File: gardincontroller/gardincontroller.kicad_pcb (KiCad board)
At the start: 2 copper layers, 26.8 x 41 mm, 24 parts, among them J1 Conn_01x04_Male, J2 USB_C_Receptacle_USB2.0, J3 Conn_01x10_Male, J4 Conn_01x06_Male, U1 ESP32-S2-MINI-1-N4, U2 LM1117-3.3

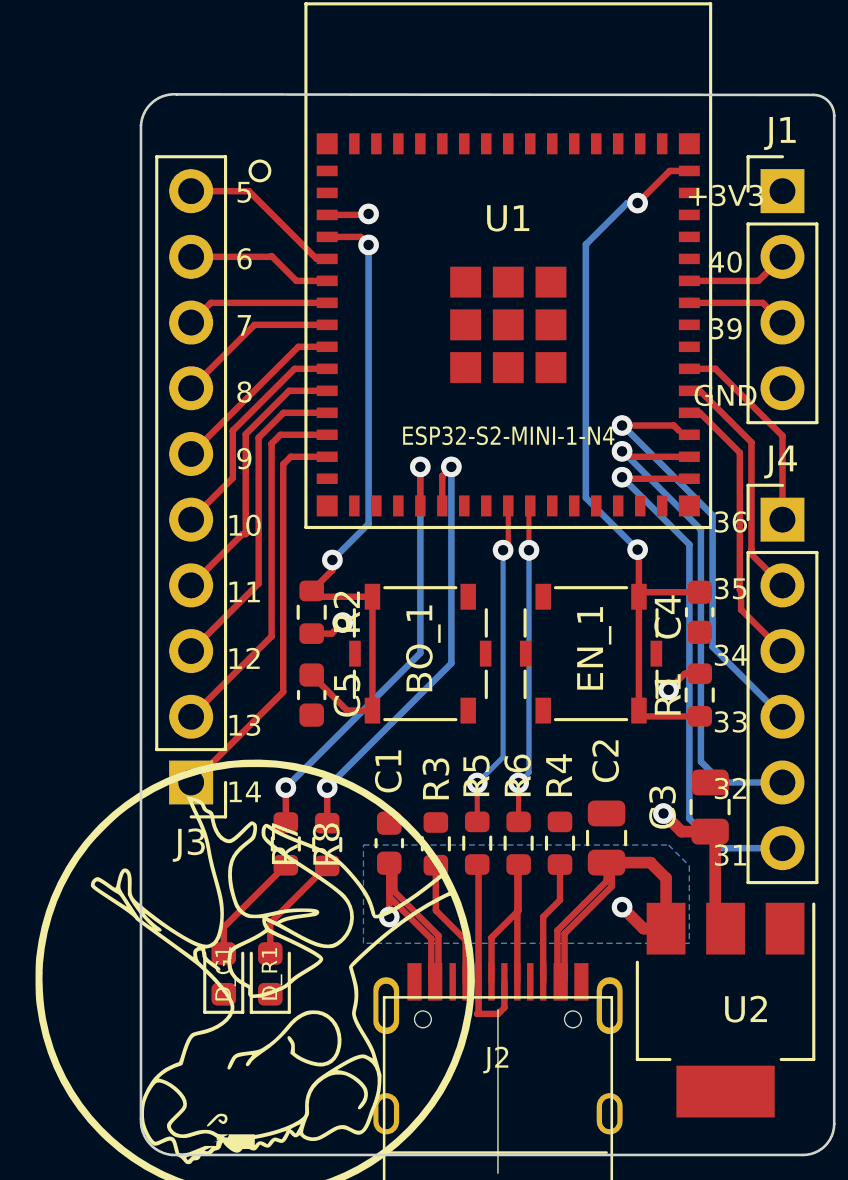
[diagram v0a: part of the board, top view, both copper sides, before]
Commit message: 11 pin header istedet
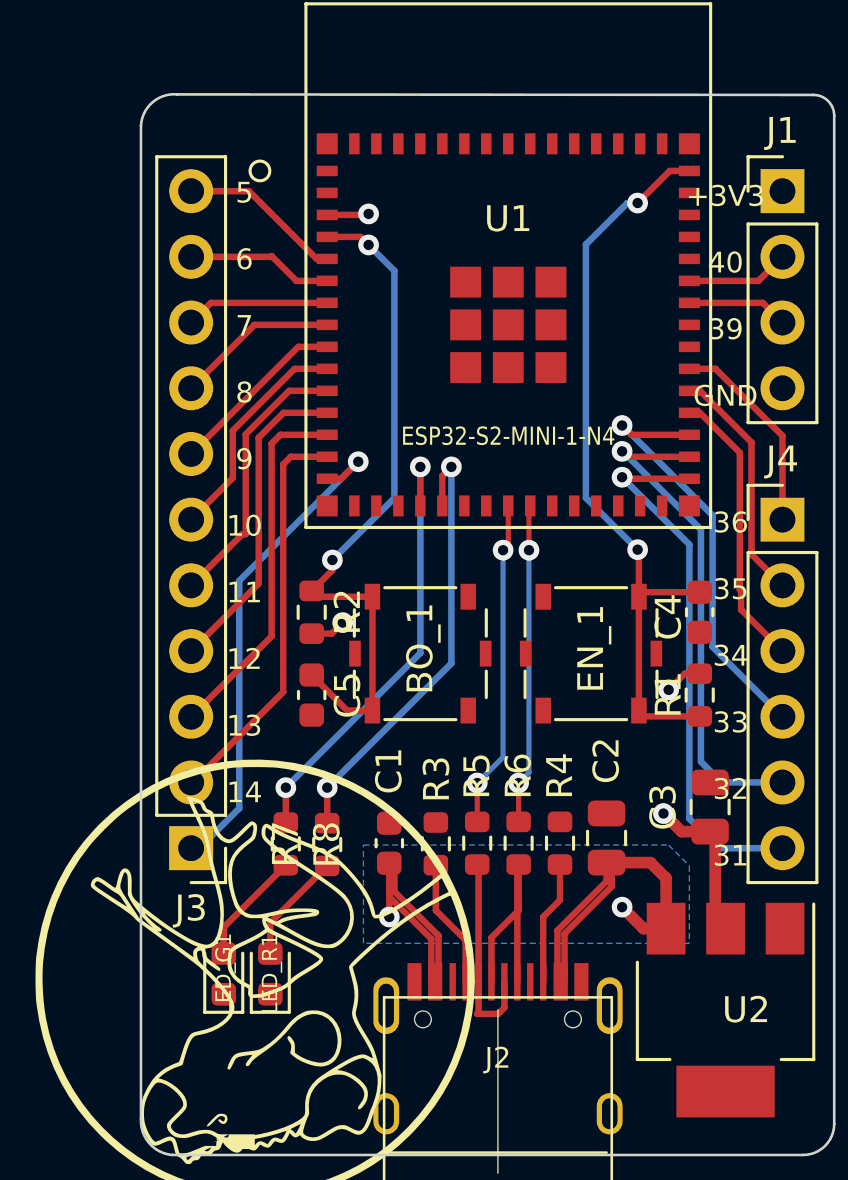
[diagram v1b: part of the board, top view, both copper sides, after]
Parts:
- J3: footprint Connector_PinHeader_2.54mm:PinHeader_1x10_P2.54mm_Vertical -> Connector_PinHeader_2.54mm:PinHeader_1x11_P2.54mm_Vertical
- moved J3 2.54 mm to (104.1, 104.1)
- renumbered D_G1 to LED_G1, D_R1 to LED_R1
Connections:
- J3 pad 1: Net-(U1-Pad14) -> Net-(J3-Pad1)
- J3 pad 10: Net-(U1-Pad5) -> Net-(U1-Pad6)
- J3 pad 2: Net-(U1-Pad13) -> Net-(U1-Pad14)
- J3 pad 3: Net-(U1-Pad12) -> Net-(U1-Pad13)
- J3 pad 4: Net-(U1-Pad11) -> Net-(U1-Pad12)
- J3 pad 5: Net-(U1-Pad10) -> Net-(U1-Pad11)
- J3 pad 6: Net-(U1-Pad9) -> Net-(U1-Pad10)
- J3 pad 7: Net-(U1-Pad8) -> Net-(U1-Pad9)
- J3 pad 8: Net-(U1-Pad7) -> Net-(U1-Pad8)
- J3 pad 9: Net-(U1-Pad6) -> Net-(U1-Pad7)
- U1 pad 15: unconnected-(U1-Pad15) -> Net-(J3-Pad1)
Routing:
- net Net-(J3-Pad1): track 0.00 -> 19.3 mm, vias 0 -> 1
- net /BOOT: track 25.8 -> 26.6 mm
